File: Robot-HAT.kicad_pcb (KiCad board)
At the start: 2 copper layers, 65 x 56 mm, 46 parts, among them Q1 BC817, Q2 BC817, Q3 BC817, SW1 SW_PUSH, U1 CAT24C32WI-GT3

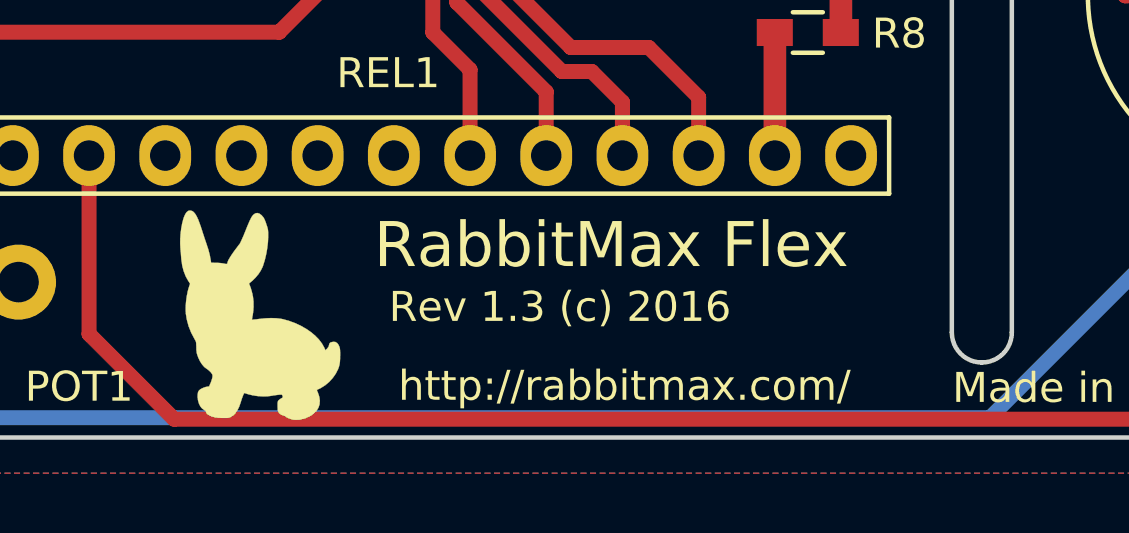
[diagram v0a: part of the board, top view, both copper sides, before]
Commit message: Robot-HAT.kicad_pcb: Update silkscreen
Signed-off-by: Leon Anavi <leon@anavi.org>
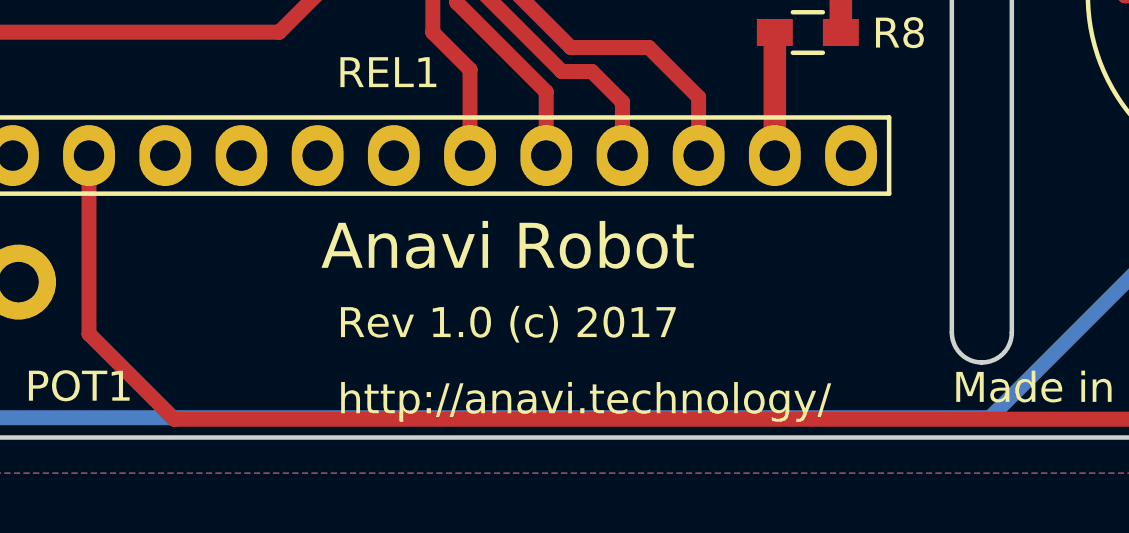
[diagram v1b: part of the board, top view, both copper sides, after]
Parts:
- removed G***: LOGO, myfootprint:logo
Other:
- board text added: "Anavi Robot"
- board text added: "Rev 1.0 (c) 2017"
- board text added: "http://anavi.technology/"
- board text removed: "RabbitMax Flex"
- board text removed: "Rev 1.3 (c) 2016"
- board text removed: "http://rabbitmax.com/"
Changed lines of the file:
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@@
     (tracks 265)
     (zones 0)
-    (modules 46)
+    (modules 45)
     (nets 54)
   )
   (page A4)
   (layers
-    (0 F.Cu signal hide)
+    (0 F.Cu signal)
     (31 B.Cu signal hide)
-    (32 B.Adhes user hide)
-    (33 F.Adhes user hide)
-    (34 B.Paste user hide)
-    (35 F.Paste user hide)
-    (36 B.SilkS user hide)
-    (37 F.SilkS user hide)
+    (32 B.Adhes user)
+    (33 F.Adhes user)
+    (34 B.Paste user)
+    (35 F.Paste user)
+    (36 B.SilkS user)
+    (37 F.SilkS user)
     (38 B.Mask user hide)
-    (39 F.Mask user hide)
+    (39 F.Mask user)
     (40 Dwgs.User user hide)
     (41 Cmts.User user hide)
@@
     (44 Edge.Cuts user)
     (45 Margin user hide)
-    (46 B.CrtYd user hide)
+    (46 B.CrtYd user)
     (47 F.CrtYd user)
     (48 B.Fab user hide)
-    (49 F.Fab user)
+    (49 F.Fab user hide)
   )
   (setup
@@
       (net 1 GND))
   )
-  (module myfootprint:logo (layer F.Cu)
-    (at 118.91 120.53)
-    (fp_text reference G*** (at 0 0) (layer F.SilkS) hide
-      (effects (font (thickness 0.3)))
-    )
-    (fp_text value LOGO (at 0.75 0) (layer F.SilkS) hide
-      (effects (font (thickness 0.3)))
-    )
-    (fp_poly (pts (xy -2.249089 -3.487442) (xy -2.230535 -3.478895) (xy -2.190613 -3.452478) (xy -2.152332 -3.414282)
-      (xy -2.114621 -3.362128) (xy -2.076406 -3.293837) (xy -2.036615 -3.207228) (xy -1.994175 -3.100123)
-      (xy -1.948014 -2.970343) (xy -1.897059 -2.815708) (xy -1.884171 -2.775207) (xy -1.85445 -2.682466)
-      (xy -1.822681 -2.585364) (xy -1.791782 -2.492694) (xy -1.764675 -2.413249) (xy -1.752205 -2.377722)
-      (xy -1.692419 -2.193054) (xy -1.645635 -2.012678) (xy -1.616821 -1.862666) (xy -1.600428 -1.756833)
-      (xy -1.438741 -1.754444) (xy -1.361664 -1.751346) (xy -1.283434 -1.744909) (xy -1.215079 -1.736192)
-      (xy -1.180587 -1.72967) (xy -1.12142 -1.717512) (xy -1.084434 -1.714734) (xy -1.065001 -1.721895)
-      (xy -1.058491 -1.739557) (xy -1.058333 -1.74448) (xy -1.048667 -1.788661) (xy -1.020067 -1.852274)
-      (xy -0.973134 -1.934381) (xy -0.908464 -2.034042) (xy -0.826659 -2.150318) (xy -0.728316 -2.28227)
-      (xy -0.654353 -2.377856) (xy -0.635261 -2.408987) (xy -0.607769 -2.463526) (xy -0.573267 -2.538408)
-      (xy -0.533145 -2.630572) (xy -0.48879 -2.736953) (xy -0.465667 -2.794) (xy -0.412433 -2.925634)
-      (xy -0.367759 -3.033724) (xy -0.330223 -3.121127) (xy -0.298405 -3.190697) (xy -0.270885 -3.24529)
-      (xy -0.246243 -3.287763) (xy -0.223059 -3.32097) (xy -0.199912 -3.347767) (xy -0.1813 -3.365759)
-      (xy -0.122109 -3.403923) (xy -0.060363 -3.414116) (xy 0.003476 -3.396425) (xy 0.068941 -3.350939)
-      (xy 0.108445 -3.310755) (xy 0.138173 -3.273696) (xy 0.164152 -3.232697) (xy 0.188683 -3.182708)
-      (xy 0.214067 -3.118675) (xy 0.242604 -3.035549) (xy 0.263462 -2.970389) (xy 0.278953 -2.919059)
-      (xy 0.28979 -2.875422) (xy 0.296756 -2.832486) (xy 0.300633 -2.783263) (xy 0.302206 -2.720764)
-      (xy 0.302257 -2.637997) (xy 0.302188 -2.624666) (xy 0.293769 -2.440544) (xy 0.271531 -2.245168)
-      (xy 0.237108 -2.04736) (xy 0.192137 -1.855938) (xy 0.138254 -1.679724) (xy 0.115446 -1.617721)
-      (xy 0.057506 -1.498155) (xy -0.022656 -1.37648) (xy -0.12025 -1.258764) (xy -0.230486 -1.151076)
-      (xy -0.29423 -1.098733) (xy -0.323374 -1.074697) (xy -0.33326 -1.057028) (xy -0.327405 -1.035417)
-      (xy -0.320529 -1.021582) (xy -0.297419 -0.967505) (xy -0.272258 -0.893666) (xy -0.247369 -0.808184)
-      (xy -0.225076 -0.719181) (xy -0.207703 -0.634774) (xy -0.204548 -0.616255) (xy -0.187303 -0.451989)
-      (xy -0.185631 -0.276931) (xy -0.199375 -0.103721) (xy -0.211881 -0.022304) (xy -0.223155 0.040481)
-      (xy -0.23226 0.092631) (xy -0.238162 0.128133) (xy -0.239889 0.140714) (xy -0.226651 0.141824)
-      (xy -0.189882 0.139445) (xy -0.134004 0.134003) (xy -0.063433 0.125925) (xy 0.010584 0.116542)
-      (xy 0.213363 0.09587) (xy 0.40471 0.088589) (xy 0.580659 0.094653) (xy 0.737243 0.114016)
-      (xy 0.793923 0.125557) (xy 0.999181 0.182276) (xy 1.197574 0.255377) (xy 1.38642 0.343026)
-      (xy 1.563038 0.443387) (xy 1.724748 0.554626) (xy 1.868868 0.674909) (xy 1.992717 0.802402)
-      (xy 2.093615 0.935269) (xy 2.165417 1.064036) (xy 2.210154 1.161461) (xy 2.261987 1.109628)
-      (xy 2.293864 1.07187) (xy 2.316292 1.034501) (xy 2.321597 1.019259) (xy 2.334612 0.963851)
-      (xy 2.349078 0.929342) (xy 2.369446 0.90857) (xy 2.398889 0.894829) (xy 2.476875 0.877418)
-      (xy 2.54365 0.885726) (xy 2.59977 0.920021) (xy 2.645792 0.98057) (xy 2.666346 1.023557)
-      (xy 2.679746 1.058368) (xy 2.689176 1.0909) (xy 2.695323 1.127152) (xy 2.69887 1.173122)
-      (xy 2.700501 1.234806) (xy 2.700901 1.318204) (xy 2.7009 1.326445) (xy 2.699046 1.446021)
-      (xy 2.692921 1.544017) (xy 2.681553 1.626883) (xy 2.66397 1.701068) (xy 2.639201 1.77302)
-      (xy 2.630294 1.794968) (xy 2.553279 1.945562) (xy 2.453238 2.087891) (xy 2.334539 2.217335)
-      (xy 2.201553 2.329273) (xy 2.058649 2.419086) (xy 2.023108 2.436957) (xy 1.922493 2.485083)
-      (xy 1.962368 2.579989) (xy 2.006886 2.715183) (xy 2.024238 2.84317) (xy 2.01474 2.96316)
-      (xy 1.978707 3.074368) (xy 1.916457 3.176005) (xy 1.828304 3.267285) (xy 1.714565 3.347418)
-      (xy 1.638162 3.387923) (xy 1.493225 3.444825) (xy 1.349402 3.477094) (xy 1.21025 3.484119)
-      (xy 1.128889 3.475696) (xy 1.047365 3.455026) (xy 0.967065 3.42266) (xy 0.905486 3.386765)
-      (xy 0.859903 3.359672) (xy 0.812429 3.340158) (xy 0.797626 3.336412) (xy 0.734776 3.311752)
-      (xy 0.6777 3.265927) (xy 0.638477 3.212125) (xy 0.62656 3.181268) (xy 0.619041 3.138266)
-      (xy 0.615196 3.077281) (xy 0.614289 3.017455) (xy 0.614518 2.949819) (xy 0.616476 2.904035)
-      (xy 0.621342 2.873737) (xy 0.630291 2.852559) (xy 0.644501 2.834136) (xy 0.649111 2.82911)
-      (xy 0.686021 2.797046) (xy 0.730639 2.767682) (xy 0.737306 2.764118) (xy 0.773271 2.743463)
-      (xy 0.787552 2.724407) (xy 0.784299 2.69718) (xy 0.77584 2.673342) (xy 0.767621 2.654443)
-      (xy 0.756452 2.64378) (xy 0.735736 2.639833) (xy 0.698874 2.64108) (xy 0.652368 2.644878)
-      (xy 0.580687 2.652925) (xy 0.499662 2.664834) (xy 0.430389 2.67734) (xy 0.28671 2.696713)
-      (xy 0.127563 2.700752) (xy -0.039323 2.6902) (xy -0.206221 2.6658) (xy -0.365404 2.628294)
-      (xy -0.481039 2.589725) (xy -0.494303 2.591031) (xy -0.508621 2.608023) (xy -0.526391 2.644611)
-      (xy -0.547539 2.69811) (xy -0.572979 2.76891) (xy -0.598959 2.846428) (xy -0.620252 2.915011)
-      (xy -0.621986 2.921) (xy -0.668343 3.05233) (xy -0.726665 3.167955) (xy -0.794779 3.264768)
-      (xy -0.870512 3.33966) (xy -0.948557 3.388132) (xy -0.983838 3.402568) (xy -1.018125 3.412204)
-      (xy -1.058434 3.417977) (xy -1.111783 3.420828) (xy -1.185186 3.421694) (xy -1.199444 3.421711)
-      (xy -1.354408 3.415047) (xy -1.490224 3.395242) (xy -1.604469 3.362747) (xy -1.666107 3.334983)
-      (xy -1.717809 3.298864) (xy -1.756557 3.255749) (xy -1.776524 3.212696) (xy -1.778 3.199424)
-      (xy -1.789634 3.181893) (xy -1.819488 3.159118) (xy -1.845027 3.144468) (xy -1.908963 3.096841)
-      (xy -1.963706 3.026589) (xy -2.007087 2.938422) (xy -2.036937 2.837048) (xy -2.051088 2.727178)
-      (xy -2.051942 2.695223) (xy -2.047975 2.611109) (xy -2.032969 2.548041) (xy -2.003389 2.499859)
-      (xy -1.9557 2.460403) (xy -1.899592 2.429752) (xy -1.841162 2.405032) (xy -1.781668 2.385316)
-      (xy -1.734406 2.374943) (xy -1.666349 2.366883) (xy -1.615187 2.245303) (xy -1.590873 2.181402)
-      (xy -1.570763 2.11731) (xy -1.558189 2.064044) (xy -1.556238 2.050499) (xy -1.553214 2.009702)
-      (xy -1.557078 1.979978) (xy -1.571367 1.951151) (xy -1.59962 1.913048) (xy -1.607481 1.903138)
-      (xy -1.650543 1.85656) (xy -1.700294 1.813464) (xy -1.734206 1.790337) (xy -1.821543 1.725477)
-      (xy -1.902012 1.635771) (xy -1.97356 1.524183) (xy -2.034132 1.393677) (xy -2.060589 1.319389)
-      (xy -2.076233 1.26329) (xy -2.086426 1.205384) (xy -2.092293 1.13685) (xy -2.094941 1.050276)
-      (xy -2.096278 0.978046) (xy -2.098764 0.926984) (xy -2.103869 0.890038) (xy -2.11306 0.860157)
-      (xy -2.127807 0.830288) (xy -2.147832 0.796276) (xy -2.263948 0.578651) (xy -2.352292 0.357237)
-      (xy -2.41316 0.131176) (xy -2.442453 -0.055254) (xy -2.449828 -0.18828) (xy -2.446137 -0.33852)
-      (xy -2.432353 -0.497665) (xy -2.409452 -0.657404) (xy -2.378409 -0.809428) (xy -2.340199 -0.945427)
-      (xy -2.336818 -0.955492) (xy -2.302156 -1.057263) (xy -2.364296 -1.151872) (xy -2.449064 -1.304628)
-      (xy -2.516234 -1.47673) (xy -2.564703 -1.664624) (xy -2.593365 -1.864753) (xy -2.596059 -1.897944)
-      (xy -2.602976 -1.988944) (xy -2.611181 -2.090602) (xy -2.619511 -2.188747) (xy -2.625065 -2.250722)
-      (xy -2.632836 -2.404318) (xy -2.629897 -2.570509) (xy -2.617087 -2.741917) (xy -2.595245 -2.911166)
-      (xy -2.565211 -3.070881) (xy -2.527822 -3.213684) (xy -2.509185 -3.269462) (xy -2.466114 -3.368579)
-      (xy -2.418658 -3.439868) (xy -2.366727 -3.483398) (xy -2.310234 -3.499233) (xy -2.249089 -3.487442)) (layer F.SilkS) (width 0.01))
-  )
   (module myfootprint:MURATA_PKM13 (layer F.Cu)
     (at 150.3 109.87)
@@
     (effects (font (size 0.75 0.75) (thickness 0.125)))
   )
-  (gr_text http://rabbitmax.com/ (at 131.09 122.88) (layer F.SilkS)
+  (gr_text http://anavi.technology/ (at 129.75 123.33) (layer F.SilkS)
     (effects (font (size 1 1) (thickness 0.25)))
   )
-  (gr_text "Rev 1.3 (c) 2016" (at 128.94 120.25) (layer F.SilkS)
+  (gr_text "Rev 1.0 (c) 2017" (at 127.21 120.79) (layer F.SilkS)
     (effects (font (size 1 1) (thickness 0.25)))
   )
-  (gr_text "RabbitMax Flex\n" (at 130.65 118.19) (layer F.SilkS)
+  (gr_text "Anavi Robot\n" (at 127.21 118.25) (layer F.SilkS)
     (effects (font (size 1.5 1.5) (thickness 0.3)))
   )
